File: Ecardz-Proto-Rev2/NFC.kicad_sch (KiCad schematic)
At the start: 12 parts, among them IC1 M24LR04E-RMN6T/2

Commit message: most of layout complete
switched ADC pins for ease of layout. added LEDs
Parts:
- removed R22: DNP, Resistor_SMD:R_0603_1608Metric_Pad0.98x0.95mm_HandSolder, symbol Device:R_US
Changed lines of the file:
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@@
-	)
-	(junction
-		(at 109.22 34.29)
-		(diameter 0)
-		(color 0 0 0 0)
 	)
 	(junction
@@
 	(wire
 		(pts
-			(xy 97.79 34.29) (xy 97.79 31.75)
-		)
-		(stroke
-			(width 0)
-			(type default)
-		)
-	)
-	(wire
-		(pts
 			(xy 196.85 88.9) (xy 196.85 90.17)
 		)
@@
 	(wire
 		(pts
-			(xy 97.79 22.86) (xy 97.79 24.13)
-		)
-		(stroke
-			(width 0)
-			(type default)
-		)
-	)
-	(wire
-		(pts
 			(xy 177.8 36.83) (xy 193.04 36.83)
 		)
@@
 		(pts
 			(xy 204.47 29.21) (xy 204.47 25.4)
-		)
-		(stroke
-			(width 0)
-			(type default)
-		)
-	)
-	(wire
-		(pts
-			(xy 109.22 34.29) (xy 97.79 34.29)
 		)
 		(stroke
@@
 	)
 	(symbol
-		(lib_id "Device:R_US")
-		(at 97.79 27.94 180)
-		(unit 1)
-		(exclude_from_sim no)
-		(in_bom yes)
-		(on_board yes)
-		(dnp yes)
-		(fields_autoplaced yes)
-		(property "Reference" "R22"
-			(at 100.33 26.6699 0)
-			(effects
-				(font
-					(size 1.27 1.27)
-				)
-				(justify right)
-			)
-		)
-		(property "Value" "DNP"
-			(at 100.33 29.2099 0)
-			(effects
-				(font
-					(size 1.27 1.27)
-				)
-				(justify right)
-			)
-		)
-		(property "Footprint" "Resistor_SMD:R_0603_1608Metric_Pad0.98x0.95mm_HandSolder"
-			(at 96.774 27.686 90)
-			(effects
-				(font
-					(size 1.27 1.27)
-				)
-				(hide yes)
-			)
-		)
-		(property "Datasheet" "https://www.yageo.com/upload/media/product/products/datasheet/rchip/PYu-RC_Group_51_RoHS_L_12.pdf"
-			(at 97.79 27.94 0)
-			(effects
-				(font
-					(size 1.27 1.27)
-				)
-				(hide yes)
-			)
-		)
-		(property "Description" "Resistor, US symbol"
-			(at 97.79 27.94 0)
-			(effects
-				(font
-					(size 1.27 1.27)
-				)
-				(hide yes)
-			)
-		)
-		(property "MANUFACTURER PART NUMBER" "RC0603JR-070RL"
-			(at 97.79 27.94 0)
-			(effects
-				(font
-					(size 1.27 1.27)
-				)
-				(hide yes)
-			)
-		)
-		(property "Sim.Device" ""
-			(at 97.79 27.94 0)
-			(effects
-				(font
-					(size 1.27 1.27)
-				)
-				(hide yes)
-			)
-		)
-		(property "Sim.Pins" ""
-			(at 97.79 27.94 0)
-			(effects
-				(font
-					(size 1.27 1.27)
-				)
-				(hide yes)
-			)
-		)
-		(property "Sim.Type" ""
-			(at 97.79 27.94 0)
-			(effects
-				(font
-					(size 1.27 1.27)
-				)
-				(hide yes)
-			)
-		)
-		(property "Digikey Part Number" ""
-			(at 97.79 27.94 0)
-			(effects
-				(font
-					(size 1.27 1.27)
-				)
-				(hide yes)
-			)
-		)
-		(pin "1"
-		)
-		(pin "2"
-		)
-		(instances
-			(project "Ecardz-Proto"
-				(path "/2adbba85-9270-4efb-857d-656bb51406ca/95527a5c-8cb7-439d-944b-2d67c4df2ece"
-					(reference "R22")
-					(unit 1)
-				)
-			)
-		)
-	)
-	(symbol
 		(lib_name "C_1")
 		(lib_id "Device:C")
@@
 					(unit 1)
 				)
-			)
-		)
-	)
-	(symbol
-		(lib_id "power:VCC")
-		(at 97.79 22.86 0)
-		(unit 1)
-		(exclude_from_sim no)
-		(in_bom yes)
-		(on_board yes)
-		(dnp no)
-		(fields_autoplaced yes)
-		(property "Reference" "#PWR021"
-			(at 97.79 26.67 0)
-			(effects
-				(font
-					(size 1.27 1.27)
-				)
-				(hide yes)
-			)
-		)
-		(property "Value" "VDD"
-			(at 97.79 17.78 0)
-			(effects
-				(font
-					(size 1.27 1.27)
-				)
-			)
-		)
-		(property "Footprint" ""
-			(at 97.79 22.86 0)
-			(effects
-				(font
-					(size 1.27 1.27)
-				)
-				(hide yes)
-			)
-		)
-		(property "Datasheet" ""
-			(at 97.79 22.86 0)
-			(effects
-				(font
-					(size 1.27 1.27)
-				)
-				(hide yes)
-			)
-		)
-		(property "Description" "Power symbol creates a global label with name \"VCC\""
-			(at 97.79 22.86 0)
-			(effects
-				(font
-					(size 1.27 1.27)
-				)
-				(hide yes)
-			)
-		)
-		(pin "1"
-		)
-		(instances
-			(project "Ecardz-Proto"
-				(path "/2adbba85-9270-4efb-857d-656bb51406ca/95527a5c-8cb7-439d-944b-2d67c4df2ece"
-					(reference "#PWR021")
-					(unit 1)
-				)

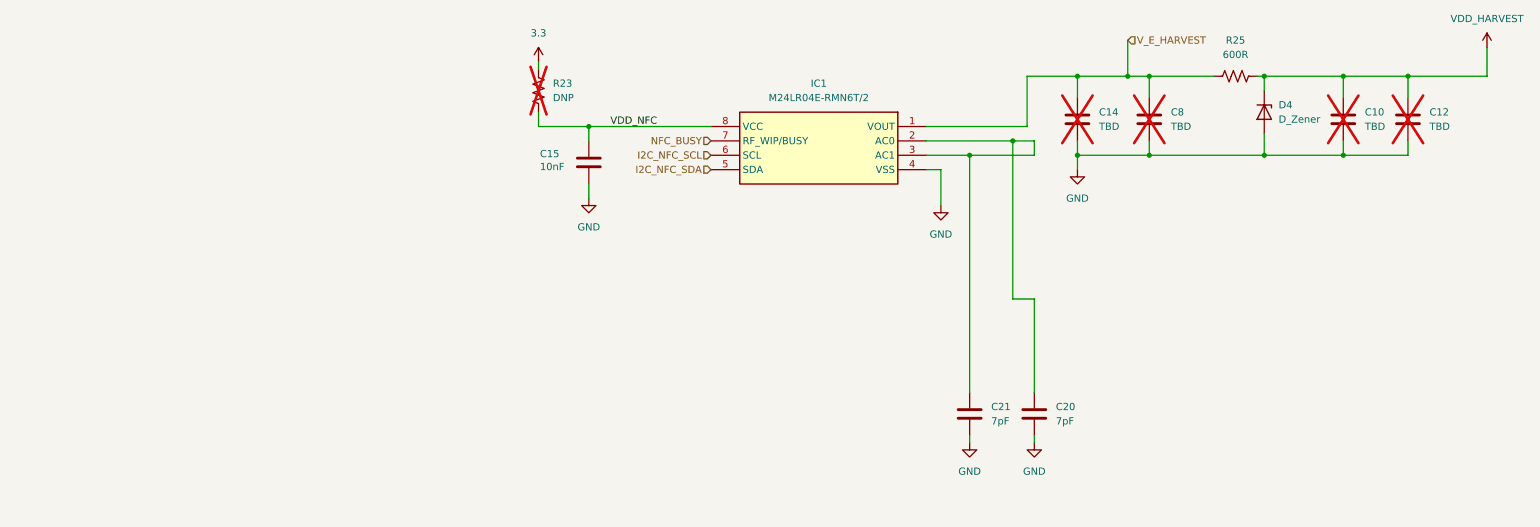
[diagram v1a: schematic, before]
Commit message: final schematic
final schematic done and BOM generated except for pogo pins and capacitors
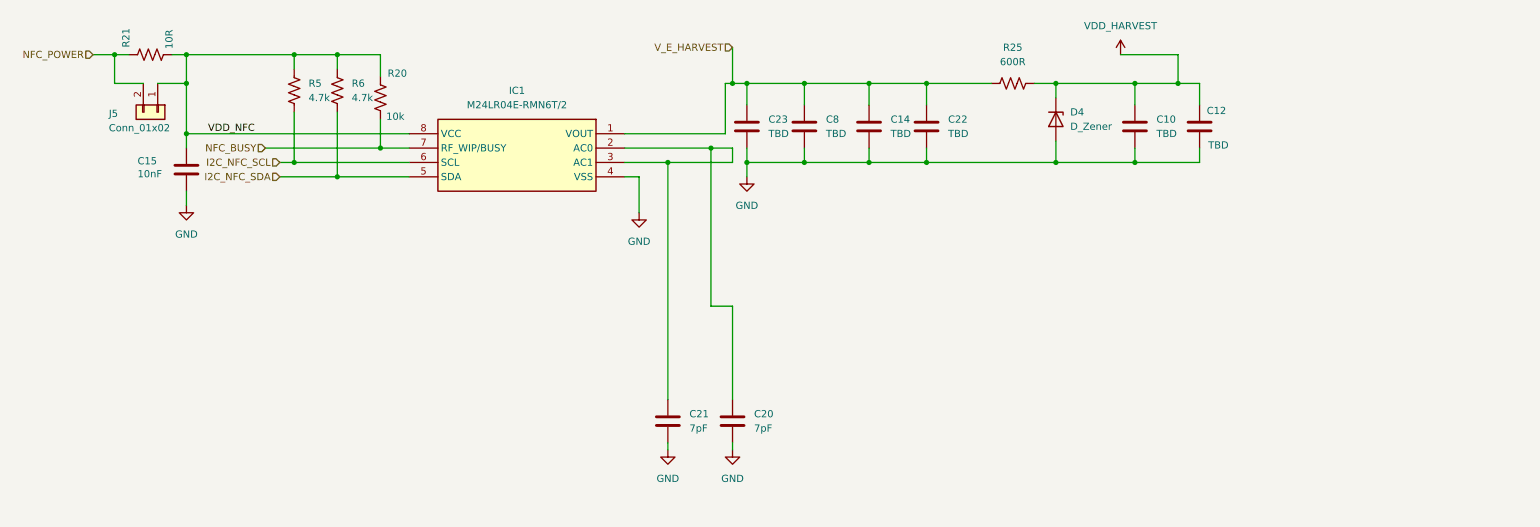
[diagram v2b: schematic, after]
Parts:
- removed R23: DNP, Resistor_SMD:R_0603_1608Metric_Pad0.98x0.95mm_HandSolder, symbol Device:R_US
- added C22: TBD, parts-lib:C_2917, symbol Device:C
- added C23: TBD, Capacitor_SMD:C_0805_2012Metric_Pad1.18x1.45mm_HandSolder, symbol Device:C
- added J5: Conn_01x02, symbol Connector_Generic:Conn_01x02
- added R20: 10k, Resistor_SMD:R_0603_1608Metric_Pad0.98x0.95mm_HandSolder, symbol Device:R_US
- added R21: 10R, Resistor_SMD:R_0603_1608Metric_Pad0.98x0.95mm_HandSolder, symbol Device:R_US
- added R5, R6: 4.7k, Resistor_SMD:R_0603_1608Metric_Pad0.98x0.95mm_HandSolder, symbol Device:R_US
- C10, C12, C14: now fitted
- C8: footprint Capacitor_SMD:C_0603_1608Metric_Pad1.08x0.95mm_HandSolder -> Capacitor_SMD:C_0805_2012Metric_Pad1.18x1.45mm_HandSolder; now fitted
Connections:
- net GND: now also C22.2, C23.2
- net I2C_NFC_SCL: now also R5.2
- net I2C_NFC_SDA: now also R6.2
- net NFC_BUSY: now also R20.2
- net VDD_NFC: now also J5.1 (Pin_1), R20.1, R21.2, R5.1, R6.1
- net V_E_HARVEST: now also C22.1, C23.1
- new net NFC_POWER: J5.2 (Pin_2), R21.1
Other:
- moved on the sheet: C15, C20, C21, D4, IC1, R25

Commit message: initial fit check for mech
final footprints defined and placement is mostly complete
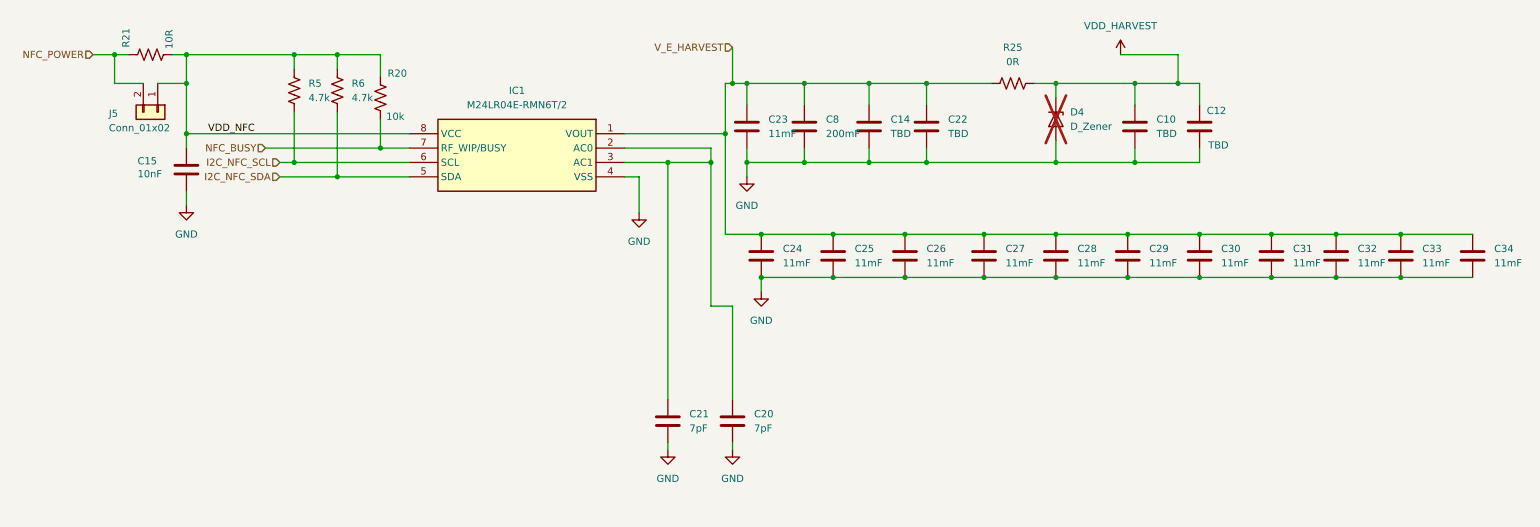
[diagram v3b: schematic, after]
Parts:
- added C24, C25, C26, C27, C28, C29, C30, C31, C32, C33, C34: 11mF, SamacSys_Parts:CPH3225A, symbol Device:C
- C23: value TBD -> 11mF; footprint Capacitor_SMD:C_0805_2012Metric_Pad1.18x1.45mm_HandSolder -> SamacSys_Parts:CPH3225A; Digikey Part Number (none) -> CPH3225A
- C8: value TBD -> 200mF; footprint Capacitor_SMD:C_0805_2012Metric_Pad1.18x1.45mm_HandSolder -> SamacSys_Parts:RSCSK2043R3D01004T; Digikey Part Number (none) -> SCSK2043R3D01004T
- D4: now not fitted
- J5: footprint (none) -> Connector_PinHeader_2.54mm:PinHeader_1x02_P2.54mm_Vertical
- R25: value 600R -> 0R
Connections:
- net GND: now also C24.2, C25.2, C26.2, C27.2, C28.2, C29.2, C30.2, C31.2, C32.2, C33.2, C34.2
- net V_E_HARVEST: now also C24.1, C25.1, C26.1, C27.1, C28.1, C29.1, C30.1, C31.1, C32.1, C33.1, C34.1

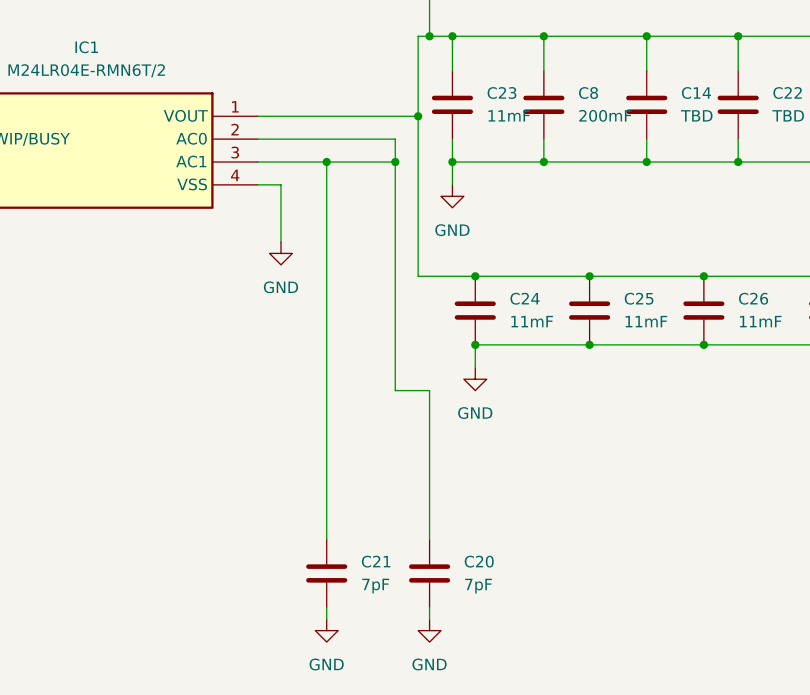
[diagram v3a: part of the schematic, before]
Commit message: added antenna jumpers
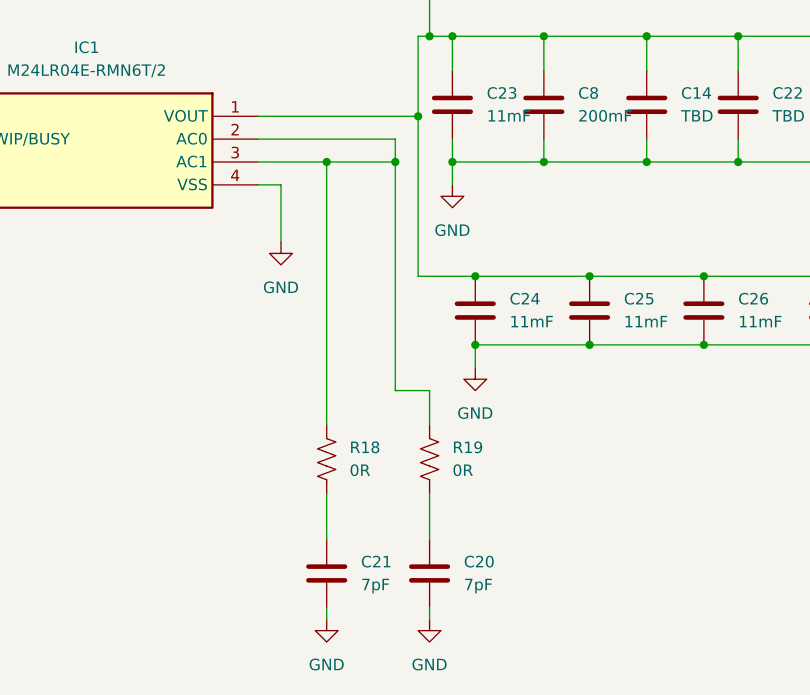
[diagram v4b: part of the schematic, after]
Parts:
- added R18, R19: 0R, Resistor_SMD:R_0603_1608Metric_Pad0.98x0.95mm_HandSolder, symbol Device:R_US
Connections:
- net at IC1.2 (AC0), IC1.3 (AC1): now also R18.2, R19.2; no longer C20.1, C21.1
- new net: C21.1, R18.1
- new net: C20.1, R19.1
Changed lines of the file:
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@@
 	(wire
 		(pts
+			(xy 132.08 77.47) (xy 132.08 82.55)
+		)
+		(stroke
+			(width 0)
+			(type default)
+		)
+	)
+	(wire
+		(pts
 			(xy 132.08 40.64) (xy 139.7 40.64)
 		)
@@
 	(wire
 		(pts
+			(xy 143.51 77.47) (xy 143.51 82.55)
+		)
+		(stroke
+			(width 0)
+			(type default)
+		)
+	)
+	(wire
+		(pts
 			(xy 238.76 53.34) (xy 250.19 53.34)
 		)
@@
 	(wire
 		(pts
-			(xy 132.08 40.64) (xy 132.08 82.55)
+			(xy 132.08 40.64) (xy 132.08 69.85)
 		)
 		(stroke
@@
 	(wire
 		(pts
-			(xy 143.51 66.04) (xy 143.51 82.55)
+			(xy 143.51 66.04) (xy 143.51 69.85)
 		)
 		(stroke
@@
 	(symbol
 		(lib_id "Device:R_US")
+		(at 132.08 73.66 180)
+		(unit 1)
+		(exclude_from_sim no)
+		(in_bom yes)
+		(on_board yes)
+		(dnp no)
+		(fields_autoplaced yes)
+		(property "Reference" "R18"
+			(at 134.62 72.3899 0)
+			(effects
+				(font
+					(size 1.27 1.27)
+				)
+				(justify right)
+			)
+		)
+		(property "Value" "0R"
+			(at 134.62 74.9299 0)
+			(effects
+				(font
+					(size 1.27 1.27)
+				)
+				(justify right)
+			)
+		)
+		(property "Footprint" "Resistor_SMD:R_0603_1608Metric_Pad0.98x0.95mm_HandSolder"
+			(at 131.064 73.406 90)
+			(effects
+				(font
+					(size 1.27 1.27)
+				)
+				(hide yes)
+			)
+		)
+		(property "Datasheet" "https://www.vishay.com/docs/20035/dcrcwe3.pdf"
+			(at 132.08 73.66 0)
+			(effects
+				(font
+					(size 1.27 1.27)
+				)
+				(hide yes)
+			)
+		)
+		(property "Description" "Resistor, US symbol"
+			(at 132.08 73.66 0)
+			(effects
+				(font
+					(size 1.27 1.27)
+				)
+				(hide yes)
+			)
+		)
+		(property "MANUFACTURER PART NUMBER" "CRCW0603590RFKEA"
+			(at 132.08 73.66 0)
+			(effects
+				(font
+					(size 1.27 1.27)
+				)
+				(hide yes)
+			)
+		)
+		(property "Digikey Part Number" "541-590HTR-ND"
+			(at 132.08 73.66 0)
+			(effects
+				(font
+					(size 1.27 1.27)
+				)
+				(hide yes)
+			)
+		)
+		(pin "1"
+		)
+		(pin "2"
+		)
+		(instances
+			(project "Ecardz-Proto"
+				(path "/2adbba85-9270-4efb-857d-656bb51406ca/95527a5c-8cb7-439d-944b-2d67c4df2ece"
+					(reference "R18")
+					(unit 1)
+				)
+			)
+		)
+	)
+	(symbol
+		(lib_id "Device:R_US")
 		(at 40.64 21.59 90)
 		(unit 1)
@@
 					(unit 1)
 				)
+			)
+		)
+	)
+	(symbol
+		(lib_id "Device:R_US")
+		(at 143.51 73.66 180)
+		(unit 1)
+		(exclude_from_sim no)
+		(in_bom yes)
+		(on_board yes)
+		(dnp no)
+		(fields_autoplaced yes)
+		(property "Reference" "R19"
+			(at 146.05 72.3899 0)
+			(effects
+				(font
+					(size 1.27 1.27)
+				)
+				(justify right)
+			)
+		)
+		(property "Value" "0R"
+			(at 146.05 74.9299 0)
+			(effects
+				(font
+					(size 1.27 1.27)
+				)
+				(justify right)
+			)
+		)
+		(property "Footprint" "Resistor_SMD:R_0603_1608Metric_Pad0.98x0.95mm_HandSolder"
+			(at 142.494 73.406 90)
+			(effects
+				(font
+					(size 1.27 1.27)
+				)
+				(hide yes)
+			)
+		)
+		(property "Datasheet" "https://www.vishay.com/docs/20035/dcrcwe3.pdf"
+			(at 143.51 73.66 0)
+			(effects
+				(font
+					(size 1.27 1.27)
+				)
+				(hide yes)
+			)
+		)
+		(property "Description" "Resistor, US symbol"
+			(at 143.51 73.66 0)
+			(effects
+				(font
+					(size 1.27 1.27)
+				)
+				(hide yes)
+			)
+		)
+		(property "MANUFACTURER PART NUMBER" "CRCW0603590RFKEA"
+			(at 143.51 73.66 0)
+			(effects
+				(font
+					(size 1.27 1.27)
+				)
+				(hide yes)
+			)
+		)
+		(property "Digikey Part Number" "541-590HTR-ND"
+			(at 143.51 73.66 0)
+			(effects
+				(font
+					(size 1.27 1.27)
+				)
+				(hide yes)
+			)
+		)
+		(pin "1"
+		)
+		(pin "2"
+		)
+		(instances
+			(project "Ecardz-Proto"
+				(path "/2adbba85-9270-4efb-857d-656bb51406ca/95527a5c-8cb7-439d-944b-2d67c4df2ece"
+					(reference "R19")
+					(unit 1)
+				)

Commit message: second mech spin
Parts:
- J5: now not fitted
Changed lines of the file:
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@@
 		(in_bom yes)
 		(on_board yes)
-		(dnp no)
+		(dnp yes)
 		(property "Reference" "J5"
 			(at 33.274 32.004 90)

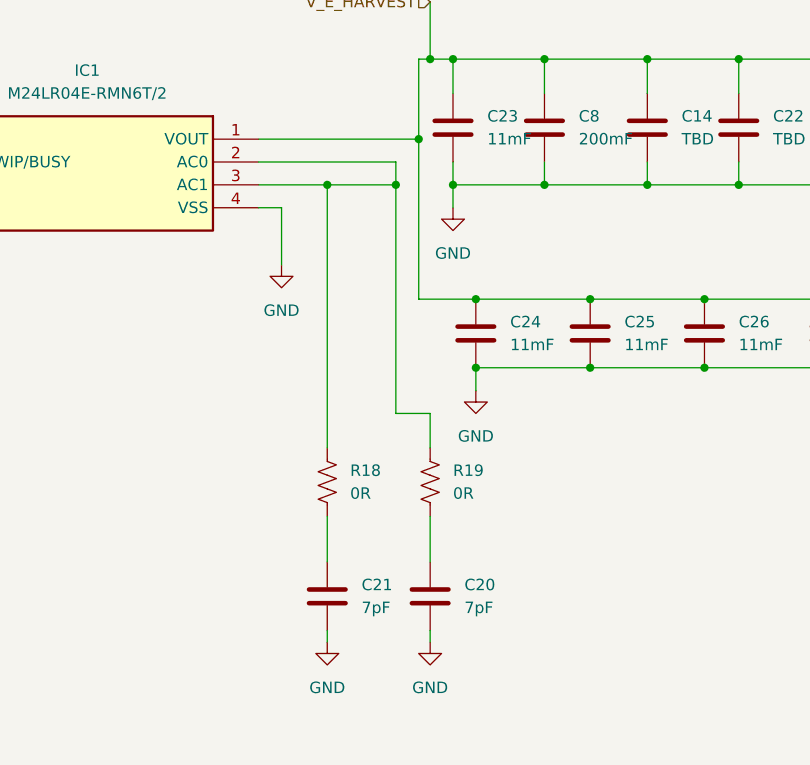
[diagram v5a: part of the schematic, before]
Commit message: all tracks connected
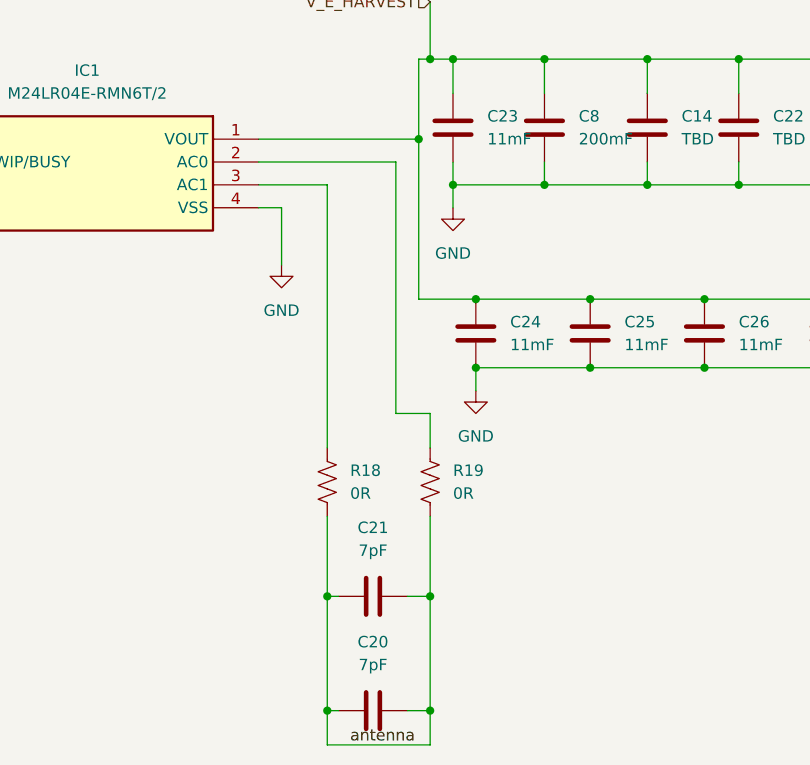
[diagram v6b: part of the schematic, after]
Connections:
- net GND: no longer C20.2, C21.2
- net antenna: now reaches C21.1, R18.1
- net antenna: now also C20.1, C20.2, C21.2, R19.1
- net at IC1.3 (AC1), R18.2: no longer IC1.2 (AC0), R19.2
- new net: IC1.2 (AC0), R19.2
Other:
- moved on the sheet: C21
